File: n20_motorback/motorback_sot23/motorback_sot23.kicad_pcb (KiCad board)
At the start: 2 copper layers, 21.4 x 11 mm, 12 parts, among them J1 Servo wire input, J2 Conn_01x01_Male, J3 Conn_01x01_Male, U1 DRV8837DSGR, U2 ATtiny4-TS, U3 AIC1734-33GUTR

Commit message: tweaks
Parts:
- moved C1 1.75 mm to (157.3, 123.2), turned to -90 degrees
- moved U3 0.35 mm to (166.5, 121.7)
- moved C2 0.05 mm to (154.8, 119.2)
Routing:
- net GND: track 25.6 -> 30.1 mm
- net BLINKY: track 8.75 -> 7.45 mm

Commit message: motorback sot23 update
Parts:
- added J4: prog_pins, motorback:pogopins_5, B.Cu at (173.5, 120.0)
- J1: footprint Connector_JST:JST_SH_SM05B-SRSS-TB_1x05-1MP_P1.00mm_Horizontal -> motorback:JST_SH_3or5
- moved U1 0.14 mm to (156.9, 116.9)
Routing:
- net /VLOGIC: track 20.7 -> 29.2 mm, vias 2 -> 3
- net /MOTORR: track 20.9 -> 26.1 mm, vias 2 -> 3
- net /MOTORF: track 21.1 -> 25.7 mm
- net PWMIN: track 6.69 -> 9.06 mm, vias 0 -> 1
- net BLINKY: track 7.45 -> 8.67 mm
- net GND: track 30.1 -> 31.2 mm
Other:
- outline, holes or cut-outs redrawn

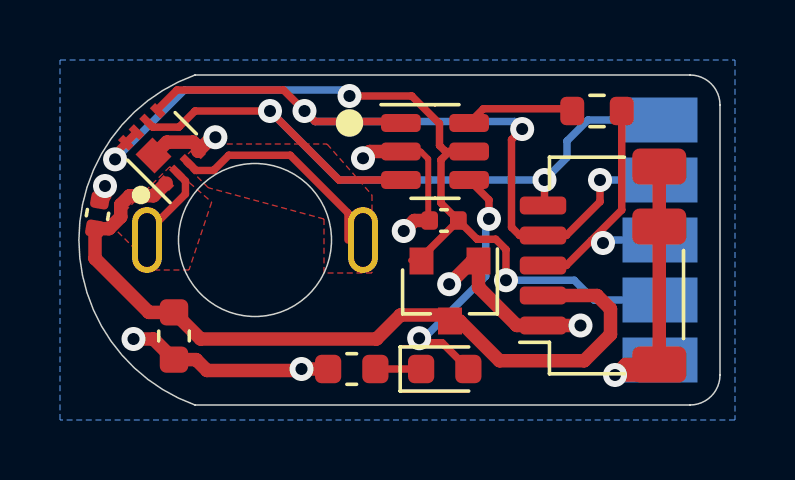
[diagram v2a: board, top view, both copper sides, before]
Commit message: More tweaks, use 3-way connector fix 3d models
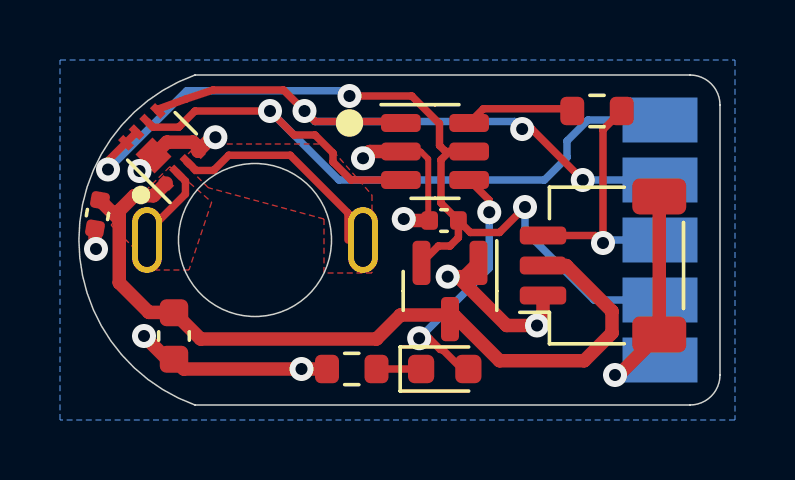
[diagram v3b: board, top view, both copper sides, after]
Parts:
- J1: footprint motorback:JST_SH_3or5 -> Connector_JST:JST_SH_SM03B-SRSS-TB_1x03-1MP_P1.00mm_Horizontal
- turned C2 to -100 degrees
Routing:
- net /MOTORR: track 26.1 -> 21.5 mm
- net GND: track 31.2 -> 28.6 mm, vias 9 -> 10
- net /VLOGIC: track 29.2 -> 30.8 mm
- net /MOTORF: track 25.7 -> 25.0 mm, vias 2 -> 1

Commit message: motorback updates
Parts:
- moved J1 0.85 mm to (171.6, 120.0)
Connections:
- J4 pad 4: /MOTORR -> /MOTORF
- J4 pad 5: /MOTORF -> /MOTORR
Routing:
- net /MOTORF: track 25.0 -> 24.0 mm
- net /VLOGIC: track 30.8 -> 31.6 mm
- net PWMIN: track 8.70 -> 7.91 mm
- net /MOTORR: track 21.5 -> 20.7 mm, vias 3 -> 1
